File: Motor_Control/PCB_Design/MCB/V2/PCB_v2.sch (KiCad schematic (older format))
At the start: 20 parts, among them J1 Molex_Motor, J2 Conn_Encoder, J3 Molex_Pwr_In, J5 Molex_Pwr_Out, J6 Adress_Pins, J9 Conn_I2C, U1 DRV8308

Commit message: Schema 2 Sophie ajout rég tension (pas bonnes pins)
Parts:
- removed R10, R9: 4.7k, Resistor_THT:R_Axial_DIN0207_L6.3mm_D2.5mm_P7.62mm_Horizontal, symbol Device:R
- added U4: LM2931AZ-5.0_TO92, Package_TO_SOT_THT:TO-92_Inline, symbol Regulator_Linear:LM2931AZ-5.0_TO92
- J1: symbol MyLibrary:Molex_39-28-1083 -> PCB_v2-rescue:Molex_39-28-1083-MyLibrary
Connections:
- wire segments 173 -> 172
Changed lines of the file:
@@
 EESchema Schematic File Version 4
 LIBS:PCB_v2-cache
-EELAYER 26 0
+EELAYER 30 0
 EELAYER END
 $Descr A4 11693 8268
@@
 Vreg
 $Comp
-L MyLibrary:Molex_39-28-1083 J1
+L PCB_v2-rescue:Molex_39-28-1083-MyLibrary J1
 U 1 1 5BE0BE2F
 P 1750 3050
@@
 Wire Wire Line
 	1050 1200 1200 1200
-$Comp
-L Device:R R9
-U 1 1 5C81C7E8
-P 8500 3050
-F 0 "R9" V 8293 3050 50  0000 C CNN
-F 1 "4.7k" V 8384 3050 50  0000 C CNN
-F 2 "Resistor_THT:R_Axial_DIN0207_L6.3mm_D2.5mm_P7.62mm_Horizontal" V 8430 3050 50  0001 C CNN
-F 3 "~" H 8500 3050 50  0001 C CNN
-	1    8500 3050
-	0    1    1    0
-$EndComp
 Wire Wire Line
 	8650 3050 9050 3050
-Text Label 8500 3850 0    50   ~ 0
-3.3V
-$Comp
-L Device:R R10
-U 1 1 5C852459
-P 8500 3450
-F 0 "R10" V 8293 3450 50  0000 C CNN
-F 1 "4.7k" V 8384 3450 50  0000 C CNN
-F 2 "Resistor_THT:R_Axial_DIN0207_L6.3mm_D2.5mm_P7.62mm_Horizontal" V 8430 3450 50  0001 C CNN
-F 3 "~" H 8500 3450 50  0001 C CNN
-	1    8500 3450
-	0    1    1    0
-$EndComp
 Wire Wire Line
 	8650 3450 9050 3450
-Wire Wire Line
-	8350 3050 8300 3050
-Wire Wire Line
-	8300 3050 8300 3450
-Wire Wire Line
-	8300 3850 8500 3850
-Wire Wire Line
-	8350 3450 8300 3450
-Connection ~ 8300 3450
-Wire Wire Line
-	8300 3450 8300 3850
 $Comp
 L power:PWR_FLAG #FLG0102
@@
 Wire Wire Line
 	11000 3350 11000 3700
+$Comp
+L Regulator_Linear:LM2931AZ-5.0_TO92 U4
+U 1 1 5DC616F9
+P 1500 1850
+F 0 "U4" H 1500 2092 50  0000 C CNN
+F 1 "LM2931AZ-5.0_TO92" H 1500 2001 50  0000 C CNN
+F 2 "Package_TO_SOT_THT:TO-92_Inline" H 1500 2075 50  0001 C CIN
+F 3 "http://www.ti.com/lit/ds/symlink/lm2931-n.pdf" H 1500 1800 50  0001 C CNN
+	1    1500 1850
+	1    0    0    -1
+$EndComp
+Wire Wire Line
+	1500 2150 1500 2250
+Wire Wire Line
+	1500 2250 1200 2250
+Text Label 1200 2250 0    50   ~ 0
+GNDREF
+Wire Wire Line
+	1200 1850 850  1850
+Text Label 850  1850 0    50   ~ 0
+Vm
+Wire Wire Line
+	1800 1850 2150 1850
+Text Label 2150 1850 2    50   ~ 0
+Vin
 $EndSCHEMATC

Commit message: Schema 2 Manu ajout LED
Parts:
- added 330ohm: R10, symbol Device:R
- added 330ohm: R11, symbol Device:R
- added 330ohm: R13, symbol Device:R
- added Rouge: LED2, symbol Device:LED
- added Rouge: LED3, symbol Device:LED
- added Vert: LED1, symbol Device:LED
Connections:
- net labels added: LED1, LED2, LED3
- wire segments 172 -> 181
- no-connect marks 15 -> 12
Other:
- note added: "Connector of the LEDs"
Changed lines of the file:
@@
 Text Label 10350 2250 2    50   ~ 0
 GNDREF
-NoConn ~ 10050 2450
-NoConn ~ 10050 2550
-NoConn ~ 10050 2650
 NoConn ~ 10050 2750
 NoConn ~ 10050 3050
@@
 Text Label 2150 1850 2    50   ~ 0
 Vin
+Wire Wire Line
+	10050 2450 10350 2450
+Wire Wire Line
+	10050 2550 10350 2550
+Wire Wire Line
+	10050 2650 10350 2650
+$Comp
+L Device:LED Vert
+U 1 1 5DCA1693
+P 10500 5500
+F 0 "Vert" H 10493 5245 50  0000 C CNN
+F 1 "LED1" H 10493 5336 50  0000 C CNN
+F 2 "" H 10500 5500 50  0001 C CNN
+F 3 "~" H 10500 5500 50  0001 C CNN
+	1    10500 5500
+	-1   0    0    1
+$EndComp
+$Comp
+L Device:LED Rouge
+U 1 1 5DCB8BC5
+P 10500 5900
+F 0 "Rouge" H 10493 5645 50  0000 C CNN
+F 1 "LED2" H 10493 5736 50  0000 C CNN
+F 2 "" H 10500 5900 50  0001 C CNN
+F 3 "~" H 10500 5900 50  0001 C CNN
+	1    10500 5900
+	-1   0    0    1
+$EndComp
+$Comp
+L Device:LED Rouge
+U 1 1 5DCC2745
+P 10500 6350
+F 0 "Rouge" H 10493 6095 50  0000 C CNN
+F 1 "LED3" H 10493 6186 50  0000 C CNN
+F 2 "" H 10500 6350 50  0001 C CNN
+F 3 "~" H 10500 6350 50  0001 C CNN
+	1    10500 6350
+	-1   0    0    1
+$EndComp
+Text Label 10800 5500 0    50   ~ 0
+GNDREF
+Text Label 10150 2450 0    50   ~ 0
+LED1
+Text Label 10150 2550 0    50   ~ 0
+LED2
+Text Label 10150 2650 0    50   ~ 0
+LED3
+Wire Wire Line
+	10650 5500 11100 5500
+Wire Wire Line
+	10650 5900 11100 5900
+Wire Wire Line
+	10650 6350 11100 6350
+Text Label 10800 5900 0    50   ~ 0
+GNDREF
+Text Label 10800 6350 0    50   ~ 0
+GNDREF
+$Comp
+L Device:R 330ohm
+U 1 1 5DDD767E
+P 10200 5500
+F 0 "330ohm" V 9993 5500 50  0000 C CNN
+F 1 "R10" V 10084 5500 50  0000 C CNN
+F 2 "" V 10130 5500 50  0001 C CNN
+F 3 "~" H 10200 5500 50  0001 C CNN
+	1    10200 5500
+	0    1    1    0
+$EndComp
+$Comp
+L Device:R 330ohm
+U 1 1 5DDF84A9
+P 10200 5900
+F 0 "330ohm" V 9993 5900 50  0000 C CNN
+F 1 "R11" V 10084 5900 50  0000 C CNN
+F 2 "" V 10130 5900 50  0001 C CNN
+F 3 "~" H 10200 5900 50  0001 C CNN
+	1    10200 5900
+	0    1    1    0
+$EndComp
+$Comp
+L Device:R 330ohm
+U 1 1 5DE026F6
+P 10200 6350
+F 0 "330ohm" V 9993 6350 50  0000 C CNN
+F 1 "R13" V 10084 6350 50  0000 C CNN
+F 2 "" V 10130 6350 50  0001 C CNN
+F 3 "~" H 10200 6350 50  0001 C CNN
+	1    10200 6350
+	0    1    1    0
+$EndComp
+Wire Wire Line
+	10050 5500 9700 5500
+Wire Wire Line
+	10050 5900 9700 5900
+Wire Wire Line
+	10050 6350 9700 6350
+Text Notes 10000 5100 0    50   ~ 0
+Connector of the LEDs
+Text Label 9700 5500 0    50   ~ 0
+LED1
+Text Label 9700 5900 0    50   ~ 0
+LED2
+Text Label 9700 6350 0    50   ~ 0
+LED3
 $EndSCHEMATC

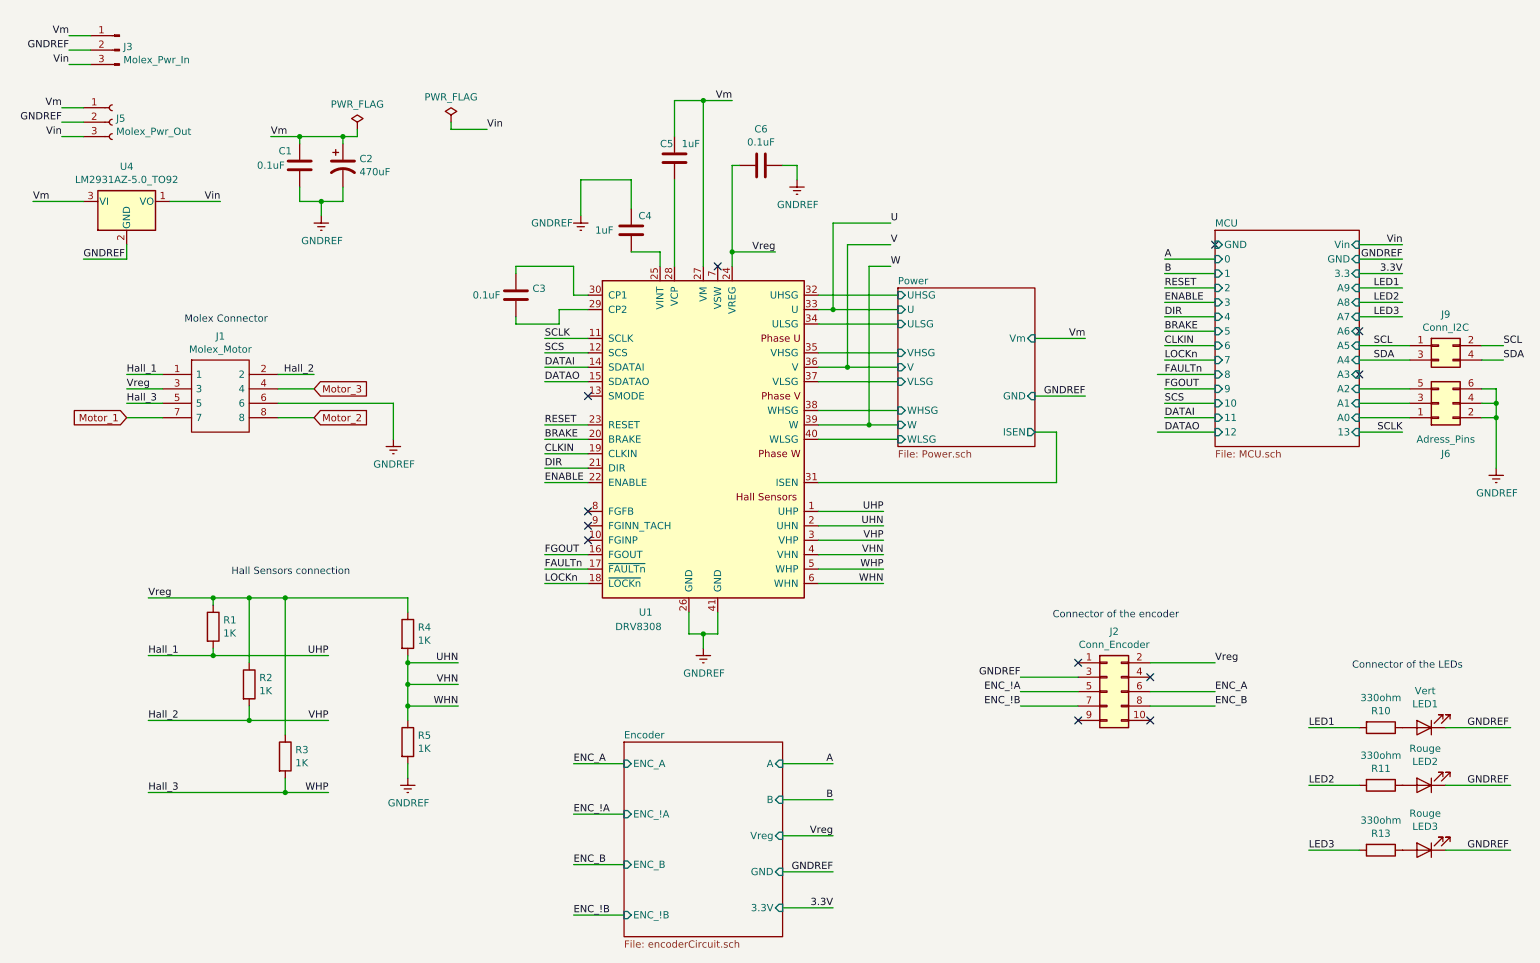
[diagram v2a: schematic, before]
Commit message: Schéma 2, modification de U2 et U3 pour les nouveaux models  + ajustement de l'orientation des connecteurs molex
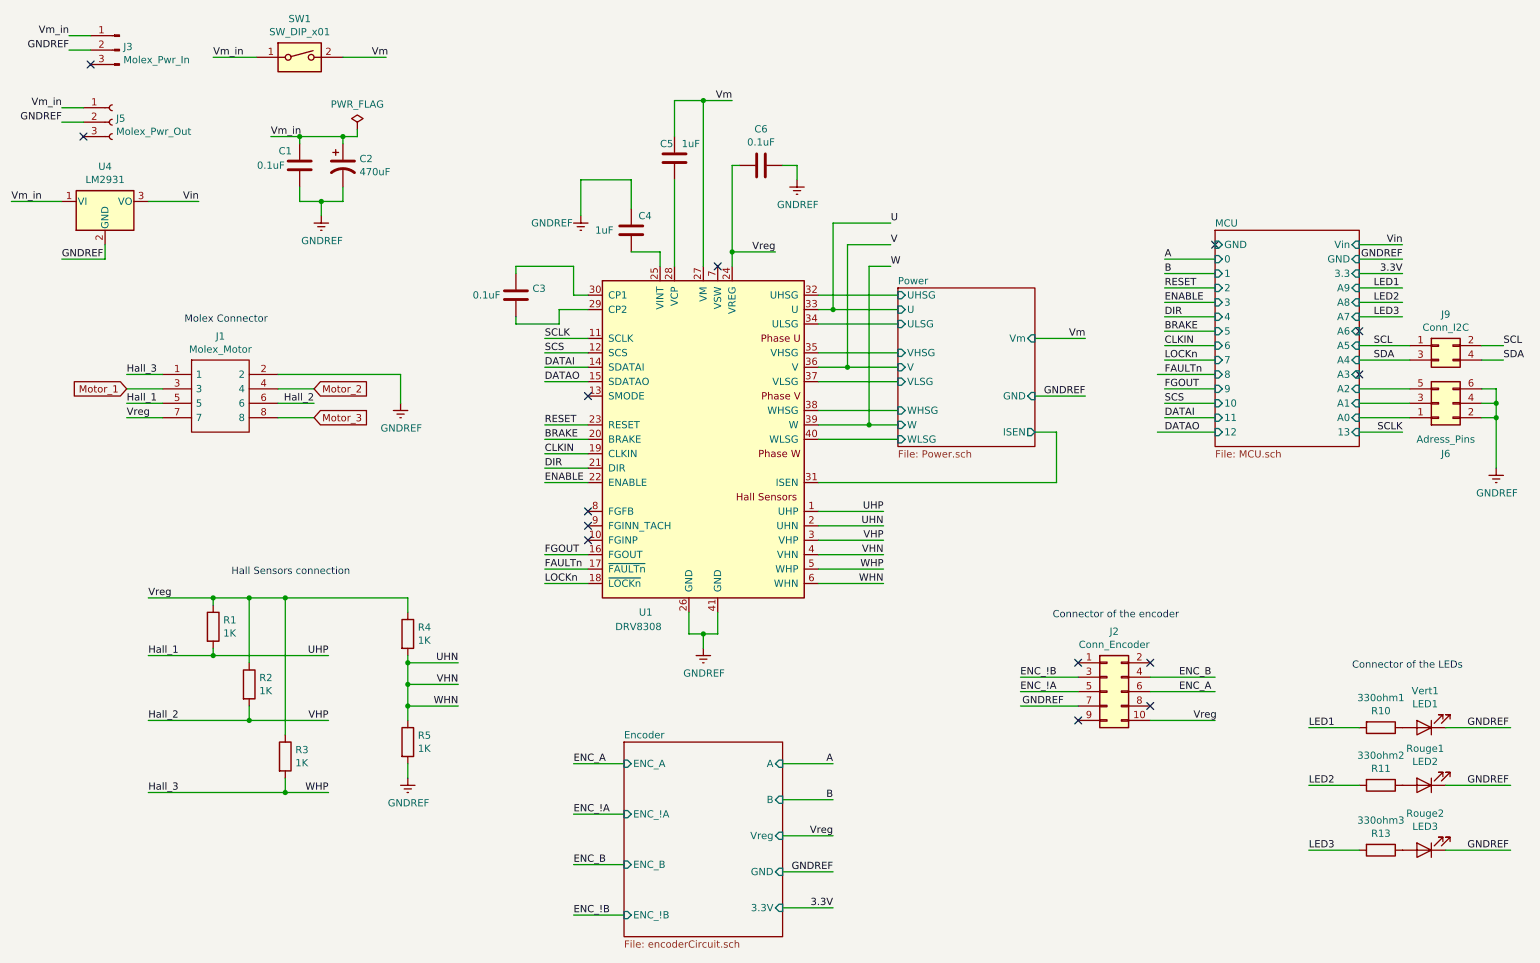
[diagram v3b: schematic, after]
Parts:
- removed U4: LM2931AZ-5.0_TO92, Package_TO_SOT_THT:TO-92_Inline, symbol Regulator_Linear:LM2931AZ-5.0_TO92
- added SW1: SW_DIP_x01, symbol Switch:SW_DIP_x01
- added U4: LM2931, Package_TO_SOT_THT:TO-92_Inline, symbol MyLibrary:LM2931
- renumbered 330ohm to 330ohm1, 330ohm to 330ohm2, 330ohm to 330ohm3, Rouge to Rouge1, Rouge to Rouge2, Vert to Vert1
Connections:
- net labels added: Vm_in
- wire segments 181 -> 179
- no-connect marks 12 -> 14
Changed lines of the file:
@@
 $EndComp
 Text Label 2500 1400 0    50   ~ 0
-Vm
+Vm_in
 Wire Wire Line
 	3100 1350 3100 1400
@@
 Wire Wire Line
 	1750 3050 1500 3050
-Wire Wire Line
-	2550 3050 2800 3050
-Text Label 1500 3050 0    50   ~ 0
+Text Label 1500 3250 0    50   ~ 0
 Hall_1
-Text Label 2800 3050 2    50   ~ 0
+Text Label 2800 3250 2    50   ~ 0
 Hall_2
 Wire Wire Line
 	1750 3150 1500 3150
-Text Label 1500 3150 0    50   ~ 0
+Text Label 1500 3350 0    50   ~ 0
 Vreg
+Text GLabel 2800 3350 2    50   Input ~ 0
+Motor_3
+Wire Wire Line
+	2550 3150 2800 3150
+Wire Wire Line
+	1750 3250 1500 3250
+Wire Wire Line
+	2550 3350 2800 3350
+Wire Wire Line
+	1750 3350 1500 3350
 Text GLabel 2800 3150 2    50   Input ~ 0
-Motor_3
-Wire Wire Line
-	2550 3150 2800 3150
-Wire Wire Line
-	1750 3250 1500 3250
-Wire Wire Line
-	2550 3350 2800 3350
-Wire Wire Line
-	1750 3350 1500 3350
-Text GLabel 2800 3350 2    50   Input ~ 0
 Motor_2
-Text GLabel 1500 3350 0    50   Input ~ 0
+Text GLabel 1500 3150 0    50   Input ~ 0
 Motor_1
-Wire Wire Line
-	2550 3250 3350 3250
-Wire Wire Line
-	3350 3250 3350 3500
 $Comp
 L power:GNDREF #PWR0106
 U 1 1 5BE1EFAA
-P 3350 3500
-F 0 "#PWR0106" H 3350 3250 50  0001 C CNN
-F 1 "GNDREF" H 3355 3327 50  0000 C CNN
-F 2 "" H 3350 3500 50  0001 C CNN
-F 3 "" H 3350 3500 50  0001 C CNN
-	1    3350 3500
-	1    0    0    -1
-$EndComp
-Text Label 1500 3250 0    50   ~ 0
+P 3400 3250
+F 0 "#PWR0106" H 3400 3000 50  0001 C CNN
+F 1 "GNDREF" H 3405 3077 50  0000 C CNN
+F 2 "" H 3400 3250 50  0001 C CNN
+F 3 "" H 3400 3250 50  0001 C CNN
+	1    3400 3250
+	1    0    0    -1
+$EndComp
+Text Label 1500 3050 0    50   ~ 0
 Hall_3
 Wire Wire Line
@@
 	1    0    0    -1
 $EndComp
-Text Label 7700 5150 2    50   ~ 0
+Text Label 8000 5350 2    50   ~ 0
 GNDREF
 Wire Wire Line
 	7700 5150 8100 5150
 NoConn ~ 8100 5050
-NoConn ~ 8600 5150
+NoConn ~ 8600 5350
 NoConn ~ 8100 5450
-NoConn ~ 8600 5450
-Text Label 9050 5050 0    50   ~ 0
+NoConn ~ 8600 5050
+Text Label 8900 5450 0    50   ~ 0
 Vreg
-Wire Wire Line
-	9050 5050 8600 5050
-Text Label 9050 5250 0    50   ~ 0
+Text Label 8800 5250 0    50   ~ 0
 ENC_A
 Wire Wire Line
 	9050 5250 8600 5250
-Text Label 9050 5350 0    50   ~ 0
+Text Label 8800 5150 0    50   ~ 0
 ENC_B
-Wire Wire Line
-	9050 5350 8600 5350
-Text Label 7700 5250 2    50   ~ 0
+Text Label 7950 5250 2    50   ~ 0
 ENC_!A
 Wire Wire Line
 	7700 5250 8100 5250
-Text Label 7700 5350 2    50   ~ 0
+Text Label 7950 5150 2    50   ~ 0
 ENC_!B
 Wire Wire Line
@@
 	1    0    0    -1
 $EndComp
-$Comp
-L Connector:Conn_01x03_Female J5
-U 1 1 5CA9A975
-P 1400 1300
-F 0 "J5" H 1427 1326 50  0000 L CNN
-F 1 "Molex_Pwr_Out" H 1427 1235 50  0000 L CNN
-F 2 "MyLibrary:Molex,1x3,Right" H 1400 1300 50  0001 C CNN
-F 3 "~" H 1400 1300 50  0001 C CNN
-	1    1400 1300
-	1    0    0    -1
-$EndComp
-Text Label 1050 1400 2    50   ~ 0
-Vin
 Text Label 1050 1300 2    50   ~ 0
 GNDREF
@@
 	1050 1300 1200 1300
 Text Label 1050 1200 2    50   ~ 0
-Vm
+Vm_in
 Wire Wire Line
 	1050 1200 1200 1200
@@
 Wire Wire Line
 	8650 3450 9050 3450
-$Comp
-L power:PWR_FLAG #FLG0102
-U 1 1 5C81F551
-P 3750 1300
-F 0 "#FLG0102" H 3750 1375 50  0001 C CNN
-F 1 "PWR_FLAG" H 3750 1474 50  0000 C CNN
-F 2 "" H 3750 1300 50  0001 C CNN
-F 3 "~" H 3750 1300 50  0001 C CNN
-	1    3750 1300
-	1    0    0    -1
-$EndComp
-Text Label 4000 1350 0    50   ~ 0
-Vin
-Wire Wire Line
-	4000 1350 3750 1350
-Wire Wire Line
-	3750 1350 3750 1300
-Wire Wire Line
-	1200 1400 1050 1400
-Text Label 1100 900  2    50   ~ 0
-Vin
 Text Label 1100 800  2    50   ~ 0
 GNDREF
@@
 	1100 800  1250 800
 Text Label 1100 700  2    50   ~ 0
-Vm
+Vm_in
 Wire Wire Line
 	1100 700  1250 700
-Wire Wire Line
-	1250 900  1100 900
 $Comp
 L Connector:Conn_01x03_Male J3
@@
 Wire Wire Line
 	11000 3350 11000 3700
-$Comp
-L Regulator_Linear:LM2931AZ-5.0_TO92 U4
-U 1 1 5DC616F9
-P 1500 1850
-F 0 "U4" H 1500 2092 50  0000 C CNN
-F 1 "LM2931AZ-5.0_TO92" H 1500 2001 50  0000 C CNN
-F 2 "Package_TO_SOT_THT:TO-92_Inline" H 1500 2075 50  0001 C CIN
-F 3 "http://www.ti.com/lit/ds/symlink/lm2931-n.pdf" H 1500 1800 50  0001 C CNN
-	1    1500 1850
-	1    0    0    -1
-$EndComp
-Wire Wire Line
-	1500 2150 1500 2250
-Wire Wire Line
-	1500 2250 1200 2250
-Text Label 1200 2250 0    50   ~ 0
+Wire Wire Line
+	1350 2150 1350 2250
+Wire Wire Line
+	1350 2250 1050 2250
+Text Label 1050 2250 0    50   ~ 0
 GNDREF
 Wire Wire Line
-	1200 1850 850  1850
-Text Label 850  1850 0    50   ~ 0
-Vm
-Wire Wire Line
-	1800 1850 2150 1850
-Text Label 2150 1850 2    50   ~ 0
+	1050 1850 700  1850
+Text Label 700  1850 0    50   ~ 0
+Vm_in
+Wire Wire Line
+	1650 1850 2000 1850
+Text Label 2000 1850 2    50   ~ 0
 Vin
 Wire Wire Line
@@
 	10050 2650 10350 2650
 $Comp
-L Device:LED Vert
+L Device:LED Vert1
 U 1 1 5DCA1693
 P 10500 5500
-F 0 "Vert" H 10493 5245 50  0000 C CNN
+F 0 "Vert1" H 10493 5245 50  0000 C CNN
 F 1 "LED1" H 10493 5336 50  0000 C CNN
 F 2 "" H 10500 5500 50  0001 C CNN
@@
 $EndComp
 $Comp
-L Device:LED Rouge
+L Device:LED Rouge1
 U 1 1 5DCB8BC5
 P 10500 5900
-F 0 "Rouge" H 10493 5645 50  0000 C CNN
+F 0 "Rouge1" H 10493 5645 50  0000 C CNN
 F 1 "LED2" H 10493 5736 50  0000 C CNN
 F 2 "" H 10500 5900 50  0001 C CNN
@@
 $EndComp
 $Comp
-L Device:LED Rouge
+L Device:LED Rouge2
 U 1 1 5DCC2745
 P 10500 6350
-F 0 "Rouge" H 10493 6095 50  0000 C CNN
+F 0 "Rouge2" H 10493 6095 50  0000 C CNN
 F 1 "LED3" H 10493 6186 50  0000 C CNN
 F 2 "" H 10500 6350 50  0001 C CNN
@@
 GNDREF
 $Comp
-L Device:R 330ohm
+L Device:R 330ohm1
 U 1 1 5DDD767E
 P 10200 5500
-F 0 "330ohm" V 9993 5500 50  0000 C CNN
+F 0 "330ohm1" V 9993 5500 50  0000 C CNN
 F 1 "R10" V 10084 5500 50  0000 C CNN
 F 2 "" V 10130 5500 50  0001 C CNN
@@
 $EndComp
 $Comp
-L Device:R 330ohm
+L Device:R 330ohm2
 U 1 1 5DDF84A9
 P 10200 5900
-F 0 "330ohm" V 9993 5900 50  0000 C CNN
+F 0 "330ohm2" V 9993 5900 50  0000 C CNN
 F 1 "R11" V 10084 5900 50  0000 C CNN
 F 2 "" V 10130 5900 50  0001 C CNN
@@
 $EndComp
 $Comp
-L Device:R 330ohm
+L Device:R 330ohm3
 U 1 1 5DE026F6
 P 10200 6350
-F 0 "330ohm" V 9993 6350 50  0000 C CNN
+F 0 "330ohm3" V 9993 6350 50  0000 C CNN
 F 1 "R13" V 10084 6350 50  0000 C CNN
 F 2 "" V 10130 6350 50  0001 C CNN
@@
 Text Label 9700 6350 0    50   ~ 0
 LED3
+$Comp
+L MyLibrary:LM2931 U4
+U 1 1 5DCAE5B5
+P 1350 1850
+F 0 "U4" H 1350 2092 50  0000 C CNN
+F 1 "LM2931" H 1350 2001 50  0000 C CNN
+F 2 "Package_TO_SOT_THT:TO-92_Inline" H 1350 2075 50  0001 C CIN
+F 3 "http://www.fairchildsemi.com/ds/LM/LM78L05A.pdf" H 1350 1800 50  0001 C CNN
+	1    1350 1850
+	1    0    0    -1
+$EndComp
+$Comp
+L Connector:Conn_01x03_Female J5
+U 1 1 5CA9A975
+P 1400 1300
+F 0 "J5" H 1427 1326 50  0000 L CNN
+F 1 "Molex_Pwr_Out" H 1427 1235 50  0000 L CNN
+F 2 "MyLibrary:Molex,1x3,Right" H 1400 1300 50  0001 C CNN
+F 3 "~" H 1400 1300 50  0001 C CNN
+	1    1400 1300
+	1    0    0    -1
+$EndComp
+NoConn ~ 1200 1400
+NoConn ~ 1250 900
+$Comp
+L Switch:SW_DIP_x01 SW1
+U 1 1 5DCCF092
+P 2700 850
+F 0 "SW1" H 2700 1117 50  0000 C CNN
+F 1 "SW_DIP_x01" H 2700 1026 50  0000 C CNN
+F 2 "" H 2700 850 50  0001 C CNN
+F 3 "~" H 2700 850 50  0001 C CNN
+	1    2700 850
+	1    0    0    -1
+$EndComp
+Wire Wire Line
+	3000 850  3300 850
+Wire Wire Line
+	2400 850  2100 850
+Text Label 2100 850  0    50   ~ 0
+Vm_in
+Text Label 3200 850  0    50   ~ 0
+Vm
+Wire Wire Line
+	2550 3250 2800 3250
+Wire Wire Line
+	3400 3050 3400 3250
+Wire Wire Line
+	2550 3050 3400 3050
+Wire Wire Line
+	8600 5450 9050 5450
+Wire Wire Line
+	8600 5150 9050 5150
 $EndSCHEMATC
